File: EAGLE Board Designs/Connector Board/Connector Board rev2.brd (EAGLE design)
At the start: 97.5 x 50.8 mm, 49 parts, among them J1 CONNECTOR-6_μF_T_V_BLACK, J10 CONNECTOR-18_MF_T_V_, J11 CONNECTOR-8_μF_T_V_BLACK, J12 CONNECTOR-8_μF_T_V_BLACK, J13 CONNECTOR-2_MF_T_V_, J14 CONNECTOR-8_μF_T_V_BLACK, J15 CONNECTOR-10_MF_T_V_, J2 CONNECTOR-8_μF_T_V_BLACK, J3 CONNECTOR-8_μF_T_V_BLACK, J4 CONNECTOR-2_MF_T_V_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

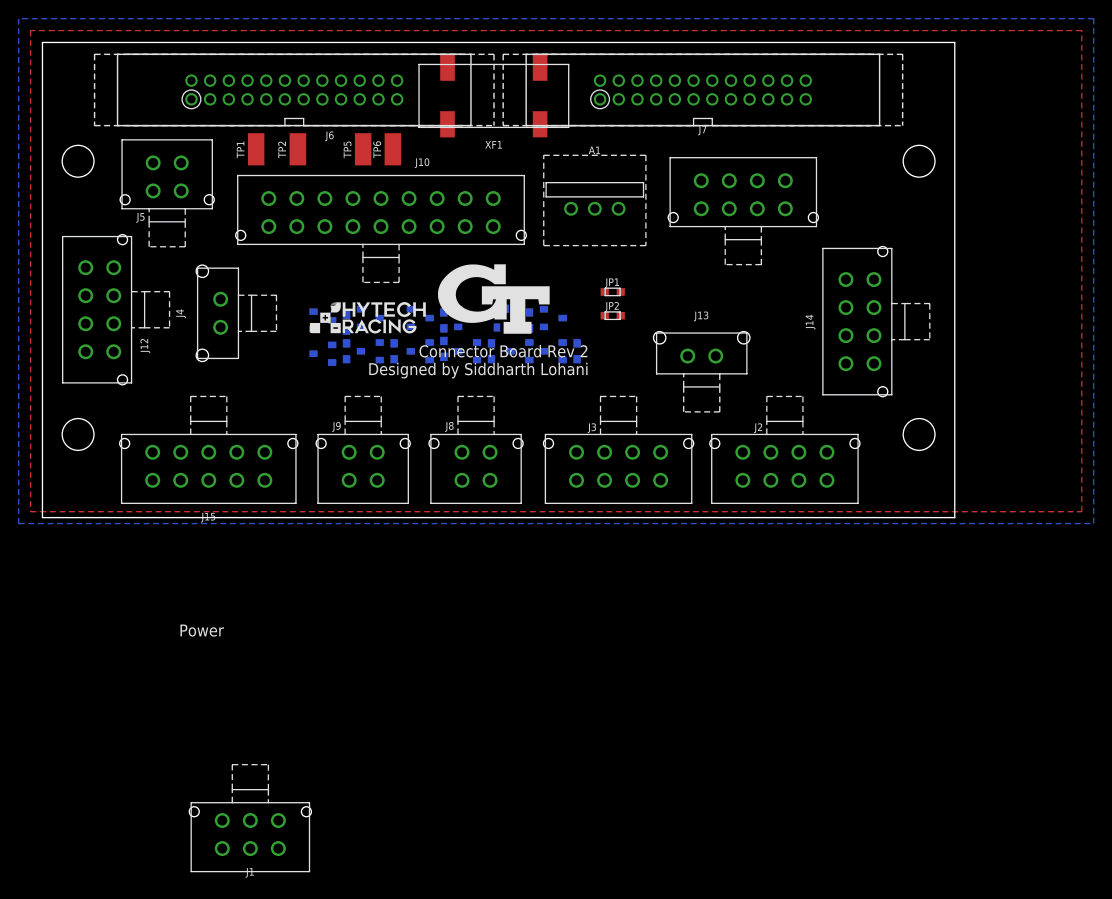
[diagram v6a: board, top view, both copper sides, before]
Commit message: shutdown signals
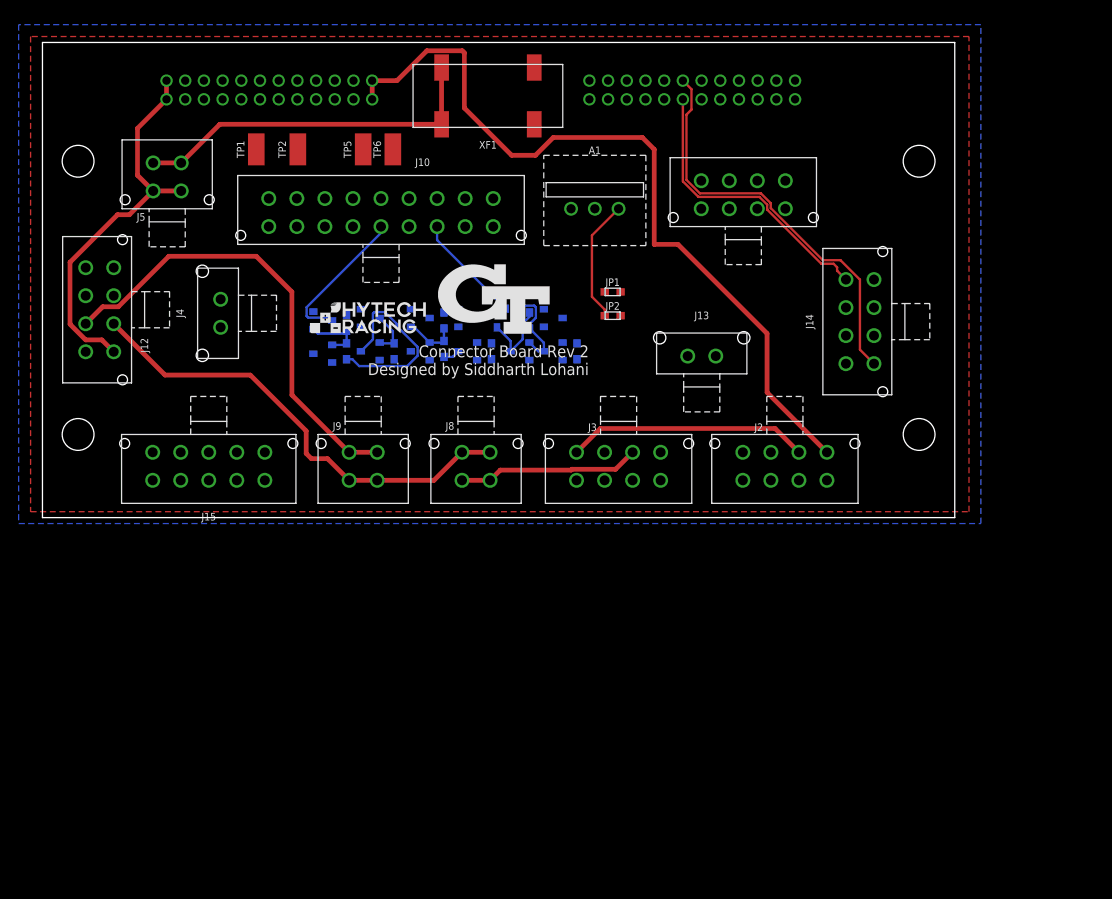
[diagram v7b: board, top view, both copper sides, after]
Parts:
- removed J1: CONNECTOR-6_μF_T_V_BLACK, HyTechDevices:MOLEX_MICROFIT_PTH_VERTICAL_06_DUAL
- moved J7 46.4 mm to (24.3, 40.6), flipped to the bottom
- moved J6 42.5 mm to (69.5, 40.6), flipped to the bottom
- moved XF1 0.63 mm to (47.6, 40.0)
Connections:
- removed net FR_CORNERN_EXT_P: J6.6
- removed net N$10: J15.4
- removed net N$12: J15.5
- removed net N$13: J15.6
- removed net N$14: J15.7
- removed net N$15: J15.8
- removed net N$6: J15.3
- net +5V: now also J15.3; no longer J1.1
- net ACCEL_1_EXT: now also J15.4; no longer J1.2
- net ACCEL_2_EXT: now also J15.5; no longer J1.3
- net BRAKE_1_EXT: now also J15.6; no longer J1.4
- net BRAKE_2_EXT: now also J15.7; no longer J1.5
- net FR_CORNER_EXT_P: now also J6.6
- net GND: now also J15.8; no longer J1.6
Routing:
- net SHDN_G: track 0.00 -> 84.4 mm
- net SHDN_J: track 0.00 -> 49.8 mm
- net SHDN_K: track 0.00 -> 49.3 mm
- net FL_CORNER_EXT_N: track 0.00 -> 45.6 mm
- net STEERING_RX_N: track 0.00 -> 44.1 mm
- net FL_CORNER_EXT_P: track 0.00 -> 43.6 mm
- net SHDN_B: track 0.00 -> 41.3 mm
- net SHDN_A: track 0.00 -> 38.6 mm
- net STEERING_TX_N: track 0.00 -> 33.0 mm
- net STEERING_TX_P: track 0.00 -> 31.7 mm
- net STEERING_RX_P: track 0.00 -> 31.1 mm
- net SHDN_H: track 0.00 -> 25.9 mm
- net FR_CORNER_EXT_P: track 0.00 -> 24.5 mm
- net FR_CORNER_EXT_N: track 0.00 -> 22.6 mm
- net +12V: track 0.00 -> 21.3 mm
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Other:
- board text removed: "Power"

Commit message: Update Connector Board rev2.brd
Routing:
- net STEERING_2_EXT: track 0.00 -> 101.0 mm
- net STEERING_1_EXT: track 0.00 -> 92.9 mm
- net CANL_3: track 0.00 -> 86.5 mm
- net CANH_3: track 0.00 -> 80.8 mm
- net ACCEL_1_EXT: track 0.00 -> 71.7 mm
- net BRAKE_1_EXT: track 0.00 -> 68.0 mm
- net ACCEL_2_EXT: track 0.00 -> 65.9 mm
- net BRAKE_2_EXT: track 0.00 -> 57.7 mm
- net CANL_2: track 0.00 -> 47.7 mm, vias 0 -> 1
- net CANH_2: track 0.00 -> 46.2 mm, vias 0 -> 1
- net FR_CORNER_EXT_P: track 24.5 -> 62.4 mm
- net LATCH_BTN: track 0.00 -> 35.2 mm
- net FR_CORNER_EXT_N: track 22.6 -> 53.6 mm
- net REFERENCE_EXT: track 0.00 -> 21.4 mm
- net SHDN_K: track 49.3 -> 70.5 mm
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- added copper zone on layer 1, net SHDN_K
